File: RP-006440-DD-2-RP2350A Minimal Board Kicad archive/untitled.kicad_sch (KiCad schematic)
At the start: 38 parts, among them J5 USB_C_Receptacle_USB2.0_16P, SW3 SW_Push, SW4 SW_Push, U4 RP2350_60QFN, U5 NCP1117-3.3_SOT223, U6 W25Q128JVS, Y2 ABM8-272-T3

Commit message: small change
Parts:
- added TP1: TestPoint, TestPoint:TestPoint_Pad_1.5x1.5mm, symbol Connector:TestPoint
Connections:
- net SWCLK: now also U4.24 (SWCLK)
- net SWDIO: now also U4.25 (SWD)
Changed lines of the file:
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@@
+	(wire
+		(pts
+			(xy 151.13 207.01) (xy 158.75 207.01)
+		)
+		(stroke
+			(width 0)
+			(type default)
+		)
+	)
 	(wire
 		(pts
@@
 		(pts
 			(xy 111.76 129.54) (xy 111.76 130.81)
+		)
+		(stroke
+			(width 0)
+			(type default)
+		)
+	)
+	(wire
+		(pts
+			(xy 151.13 204.47) (xy 158.75 204.47)
 		)
 		(stroke
@@
 		)
 	)
+	(label "SWCLK"
+		(at 151.13 204.47 0)
+		(effects
+			(font
+				(size 1.27 1.27)
+			)
+			(justify left bottom)
+		)
+	)
 	(label "QSPI_SD2"
 		(at 97.79 193.04 180)
@@
 			)
 			(justify right bottom)
+		)
+	)
+	(label "SWDIO"
+		(at 151.13 207.01 0)
+		(effects
+			(font
+				(size 1.27 1.27)
+			)
+			(justify left bottom)
 		)
 	)
@@
 					(unit 1)
 				)
+			)
+		)
+	)
+	(symbol
+		(lib_id "Connector:TestPoint")
+		(at 255.27 186.69 0)
+		(unit 1)
+		(exclude_from_sim no)
+		(in_bom yes)
+		(on_board yes)
+		(dnp no)
+		(fields_autoplaced yes)
+		(property "Reference" "TP1"
+			(at 257.81 182.1179 0)
+			(effects
+				(font
+					(size 1.27 1.27)
+				)
+				(justify left)
+			)
+		)
+		(property "Value" "TestPoint"
+			(at 257.81 184.6579 0)
+			(effects
+				(font
+					(size 1.27 1.27)
+				)
+				(justify left)
+			)
+		)
+		(property "Footprint" "TestPoint:TestPoint_Pad_1.5x1.5mm"
+			(at 260.35 186.69 0)
+			(effects
+				(font
+					(size 1.27 1.27)
+				)
+				(hide yes)
+			)
+		)
+		(property "Datasheet" "~"
+			(at 260.35 186.69 0)
+			(effects
+				(font
+					(size 1.27 1.27)
+				)
+				(hide yes)
+			)
+		)
+		(property "Description" "test point"
+			(at 255.27 186.69 0)
+			(effects
+				(font
+					(size 1.27 1.27)
+				)
+				(hide yes)
+			)
+		)
+		(pin "1"
+		)
+		(instances
+			(project ""
+				(path "/94683f5c-9cd9-448e-be96-9792537b5cb8/4bc304b2-df22-43ce-87c2-f3d7bd8364b0"
+					(reference "TP1")
+					(unit 1)
+				)

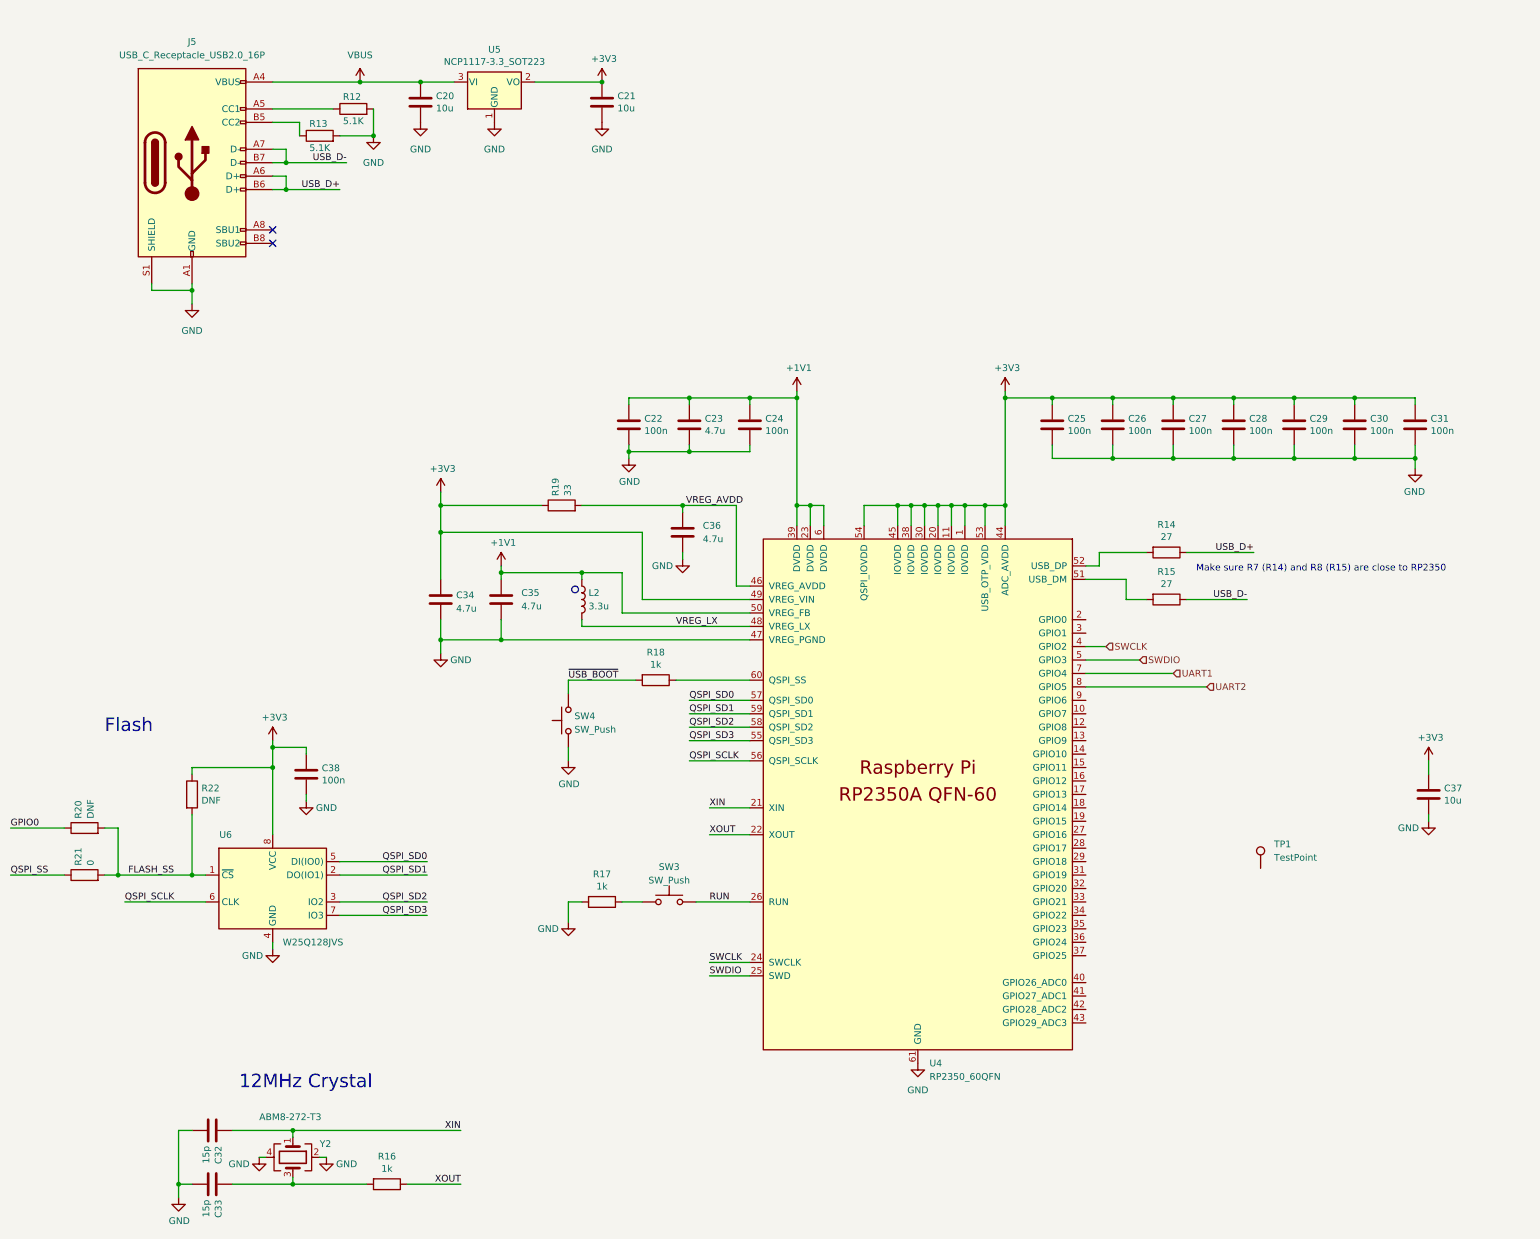
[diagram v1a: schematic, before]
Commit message: Added footprints to PCB
debugger footprints pcb
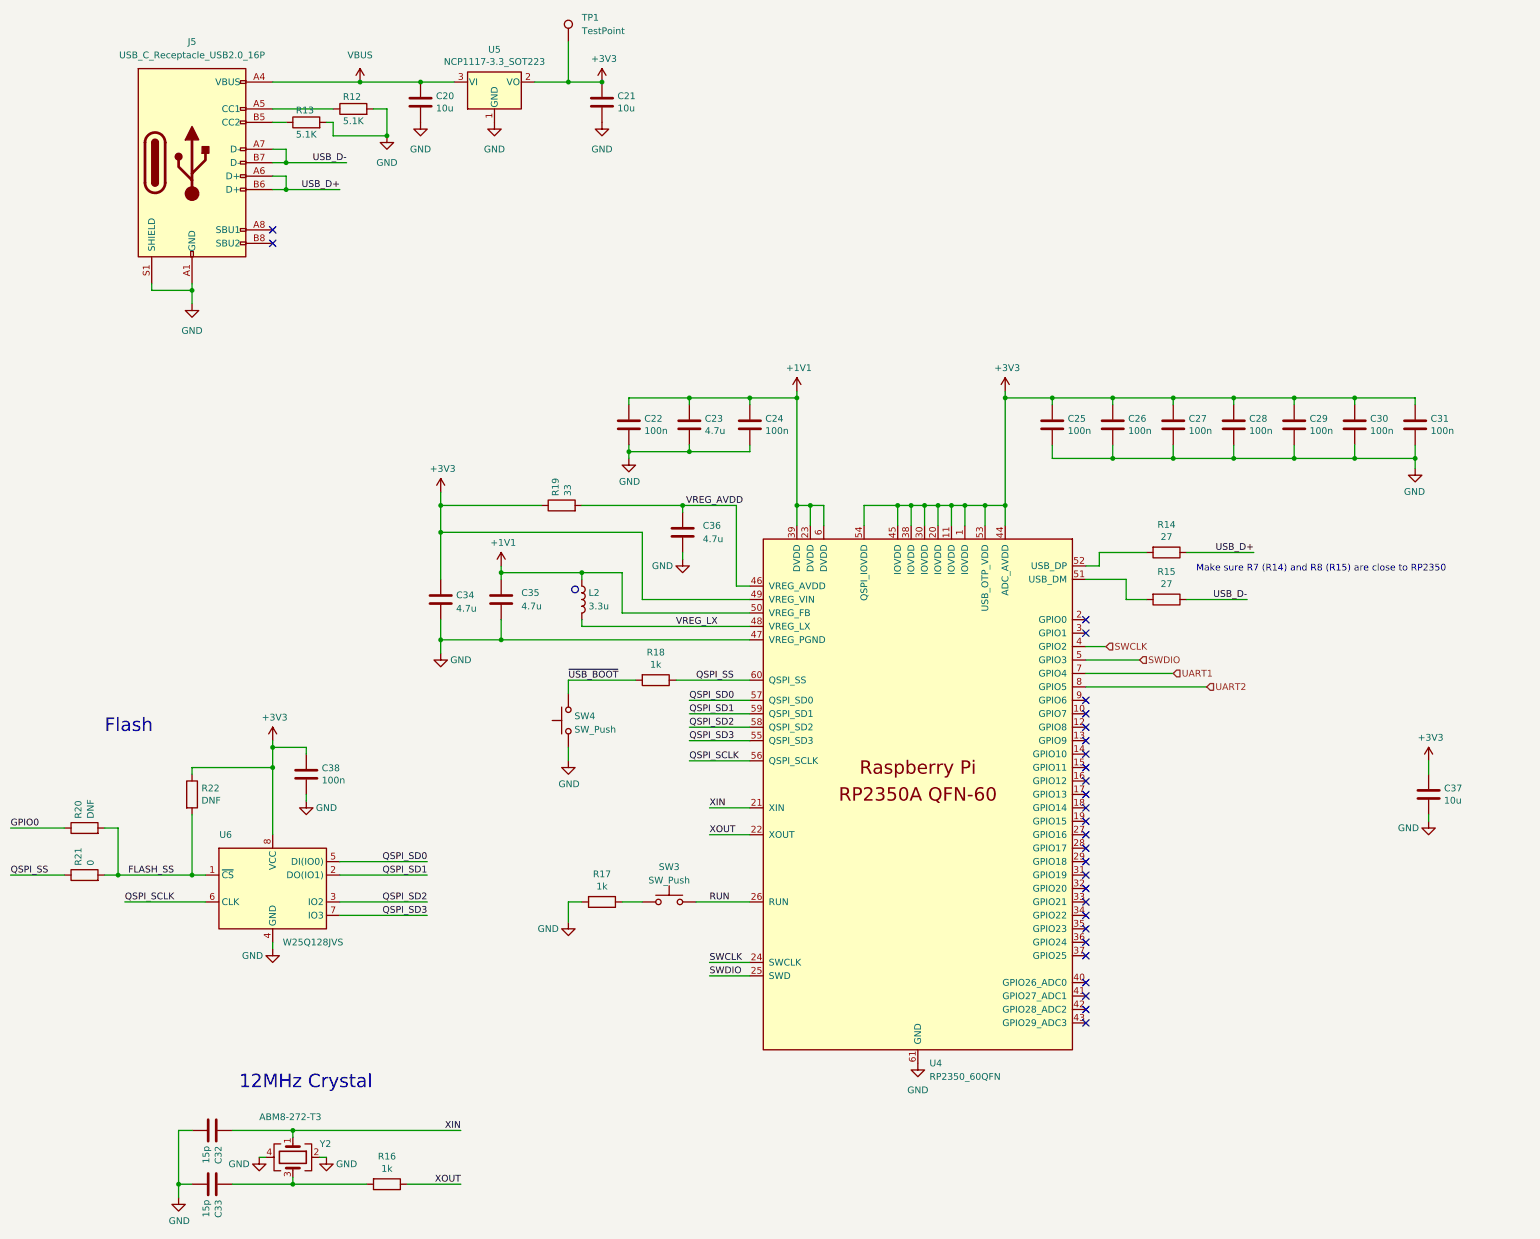
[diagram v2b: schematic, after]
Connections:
- net +3V3: now also TP1.1
- net QSPI_SS: now also R18.1, U4.60 (QSPI_SS)
- no-connect marks 2 -> 28
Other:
- moved on the sheet: R13, TP1
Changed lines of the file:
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@@
 	)
 	(junction
+		(at 90.17 48.26)
+		(diameter 0)
+		(color 0 0 0 0)
+	)
+	(junction
 		(at 158.75 97.79)
 		(diameter 0)
@@
 	)
 	(junction
+		(at 124.46 38.1)
+		(diameter 0)
+		(color 0 0 0 0)
+	)
+	(junction
 		(at 273.05 97.79)
 		(diameter 0)
@@
 	)
 	(junction
-		(at 87.63 48.26)
-		(diameter 0)
-		(color 0 0 0 0)
-	)
-	(junction
 		(at 207.01 97.79)
 		(diameter 0)
@@
 	)
 	(no_connect
+		(at 222.25 165.1)
+	)
+	(no_connect
+		(at 222.25 215.9)
+	)
+	(no_connect
+		(at 222.25 170.18)
+	)
+	(no_connect
+		(at 222.25 185.42)
+	)
+	(no_connect
+		(at 222.25 182.88)
+	)
+	(no_connect
+		(at 222.25 187.96)
+	)
+	(no_connect
+		(at 222.25 175.26)
+	)
+	(no_connect
+		(at 222.25 167.64)
+	)
+	(no_connect
+		(at 222.25 177.8)
+	)
+	(no_connect
+		(at 222.25 160.02)
+	)
+	(no_connect
+		(at 222.25 180.34)
+	)
+	(no_connect
+		(at 222.25 198.12)
+	)
+	(no_connect
+		(at 222.25 203.2)
+	)
+	(no_connect
+		(at 222.25 200.66)
+	)
+	(no_connect
+		(at 222.25 193.04)
+	)
+	(no_connect
+		(at 222.25 172.72)
+	)
+	(no_connect
+		(at 222.25 162.56)
+	)
+	(no_connect
+		(at 222.25 195.58)
+	)
+	(no_connect
+		(at 222.25 190.5)
+	)
+	(no_connect
 		(at 68.58 68.58)
 	)
 	(no_connect
+		(at 222.25 213.36)
+	)
+	(no_connect
+		(at 222.25 208.28)
+	)
+	(no_connect
+		(at 222.25 210.82)
+	)
+	(no_connect
 		(at 68.58 66.04)
 	)
+	(no_connect
+		(at 222.25 139.7)
+	)
+	(no_connect
+		(at 222.25 154.94)
+	)
+	(no_connect
+		(at 222.25 157.48)
+	)
+	(no_connect
+		(at 222.25 142.24)
+	)
 	(wire
 		(pts
@@
 	(wire
 		(pts
-			(xy 130.81 38.1) (xy 118.11 38.1)
+			(xy 130.81 38.1) (xy 124.46 38.1)
 		)
 		(stroke
@@
 	(wire
 		(pts
+			(xy 90.17 43.18) (xy 87.63 43.18)
+		)
+		(stroke
+			(width 0)
+			(type default)
+		)
+	)
+	(wire
+		(pts
 			(xy 147.32 162.56) (xy 158.75 162.56)
 		)
@@
 	(wire
 		(pts
-			(xy 87.63 48.26) (xy 87.63 43.18)
+			(xy 90.17 48.26) (xy 90.17 43.18)
 		)
 		(stroke
@@
 	(wire
 		(pts
+			(xy 80.01 45.72) (xy 80.01 48.26)
+		)
+		(stroke
+			(width 0)
+			(type default)
+		)
+	)
+	(wire
+		(pts
 			(xy 250.19 97.79) (xy 261.62 97.79)
 		)
@@
 	(wire
 		(pts
-			(xy 73.66 45.72) (xy 68.58 45.72)
+			(xy 124.46 38.1) (xy 118.11 38.1)
+		)
+		(stroke
+			(width 0)
+			(type default)
+		)
+	)
+	(wire
+		(pts
+			(xy 71.12 45.72) (xy 68.58 45.72)
 		)
 		(stroke
@@
 	(wire
 		(pts
+			(xy 124.46 30.48) (xy 124.46 38.1)
+		)
+		(stroke
+			(width 0)
+			(type default)
+		)
+	)
+	(wire
+		(pts
 			(xy 146.05 128.27) (xy 146.05 127)
 		)
@@
 	(wire
 		(pts
-			(xy 73.66 48.26) (xy 73.66 45.72)
-		)
-		(stroke
-			(width 0)
-			(type default)
-		)
-	)
-	(wire
-		(pts
 			(xy 284.48 106.68) (xy 284.48 109.22)
 		)
@@
 	(wire
 		(pts
-			(xy 81.28 48.26) (xy 87.63 48.26)
+			(xy 78.74 45.72) (xy 80.01 45.72)
 		)
 		(stroke
@@
 	(wire
 		(pts
+			(xy 80.01 48.26) (xy 90.17 48.26)
+		)
+		(stroke
+			(width 0)
+			(type default)
+		)
+	)
+	(wire
+		(pts
 			(xy 68.58 167.64) (xy 68.58 180.34)
 		)
@@
 		)
 	)
+	(label "QSPI_SS"
+		(at 148.59 151.13 0)
+		(effects
+			(font
+				(size 1.27 1.27)
+			)
+			(justify left bottom)
+		)
+	)
 	(label "USB_D-"
 		(at 252.73 135.89 180)
@@
 	(symbol
 		(lib_id "Device:R")
-		(at 77.47 48.26 90)
+		(at 74.93 45.72 90)
 		(unit 1)
 		(exclude_from_sim no)
@@
 		(dnp no)
 		(property "Reference" "R13"
-			(at 77.216 45.974 90)
+			(at 74.676 43.434 90)
 			(effects
 				(font
@@
 		)
 		(property "Value" "5.1K"
-			(at 77.47 50.546 90)
+			(at 74.93 48.006 90)
 			(effects
 				(font
@@
 		)
 		(property "Footprint" "Resistor_SMD:R_0402_1005Metric"
-			(at 77.47 50.038 90)
+			(at 74.93 47.498 90)
 			(effects
 				(font
@@
 		)
 		(property "Datasheet" "~"
-			(at 77.47 48.26 0)
+			(at 74.93 45.72 0)
 			(effects
 				(font
@@
 		)
 		(property "Description" "Resistor"
-			(at 77.47 48.26 0)
+			(at 74.93 45.72 0)
 			(effects
 				(font
@@
 	(symbol
 		(lib_id "Connector:TestPoint")
-		(at 255.27 186.69 0)
+		(at 124.46 30.48 0)
 		(unit 1)
 		(exclude_from_sim no)
@@
 		(fields_autoplaced yes)
 		(property "Reference" "TP1"
-			(at 257.81 182.1179 0)
+			(at 127 25.9079 0)
 			(effects
 				(font
@@
 		)
 		(property "Value" "TestPoint"
-			(at 257.81 184.6579 0)
+			(at 127 28.4479 0)
 			(effects
 				(font
@@
 		)
 		(property "Footprint" "TestPoint:TestPoint_Pad_1.5x1.5mm"
-			(at 260.35 186.69 0)
+			(at 129.54 30.48 0)
 			(effects
 				(font
@@
 		)
 		(property "Datasheet" "~"
-			(at 260.35 186.69 0)
+			(at 129.54 30.48 0)
 			(effects
 				(font
@@
 		)
 		(property "Description" "test point"
-			(at 255.27 186.69 0)
+			(at 124.46 30.48 0)
 			(effects
 				(font
@@
 		(lib_name "GND_1")
 		(lib_id "power:GND")
-		(at 87.63 48.26 0)
+		(at 90.17 48.26 0)
 		(unit 1)
 		(exclude_from_sim no)
@@
 		(fields_autoplaced yes)
 		(property "Reference" "#PWR038"
-			(at 87.63 54.61 0)
+			(at 90.17 54.61 0)
 			(effects
 				(font
@@
 		)
 		(property "Value" "GND"
-			(at 87.63 53.34 0)
+			(at 90.17 53.34 0)
 			(effects
 				(font
@@
 		)
 		(property "Footprint" ""
-			(at 87.63 48.26 0)
+			(at 90.17 48.26 0)
 			(effects
 				(font
@@
 		)
 		(property "Datasheet" ""
-			(at 87.63 48.26 0)
+			(at 90.17 48.26 0)
 			(effects
 				(font
@@
 		)
 		(property "Description" "Power symbol creates a global label with name \"GND\" , ground"
-			(at 87.63 48.26 0)
+			(at 90.17 48.26 0)
 			(effects
 				(font
